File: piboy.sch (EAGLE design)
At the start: 74 parts, among them CN4 MicroUSB, T1 MMUN2133LT1G, U1 TPS61090RSAR, U2 MCP73871

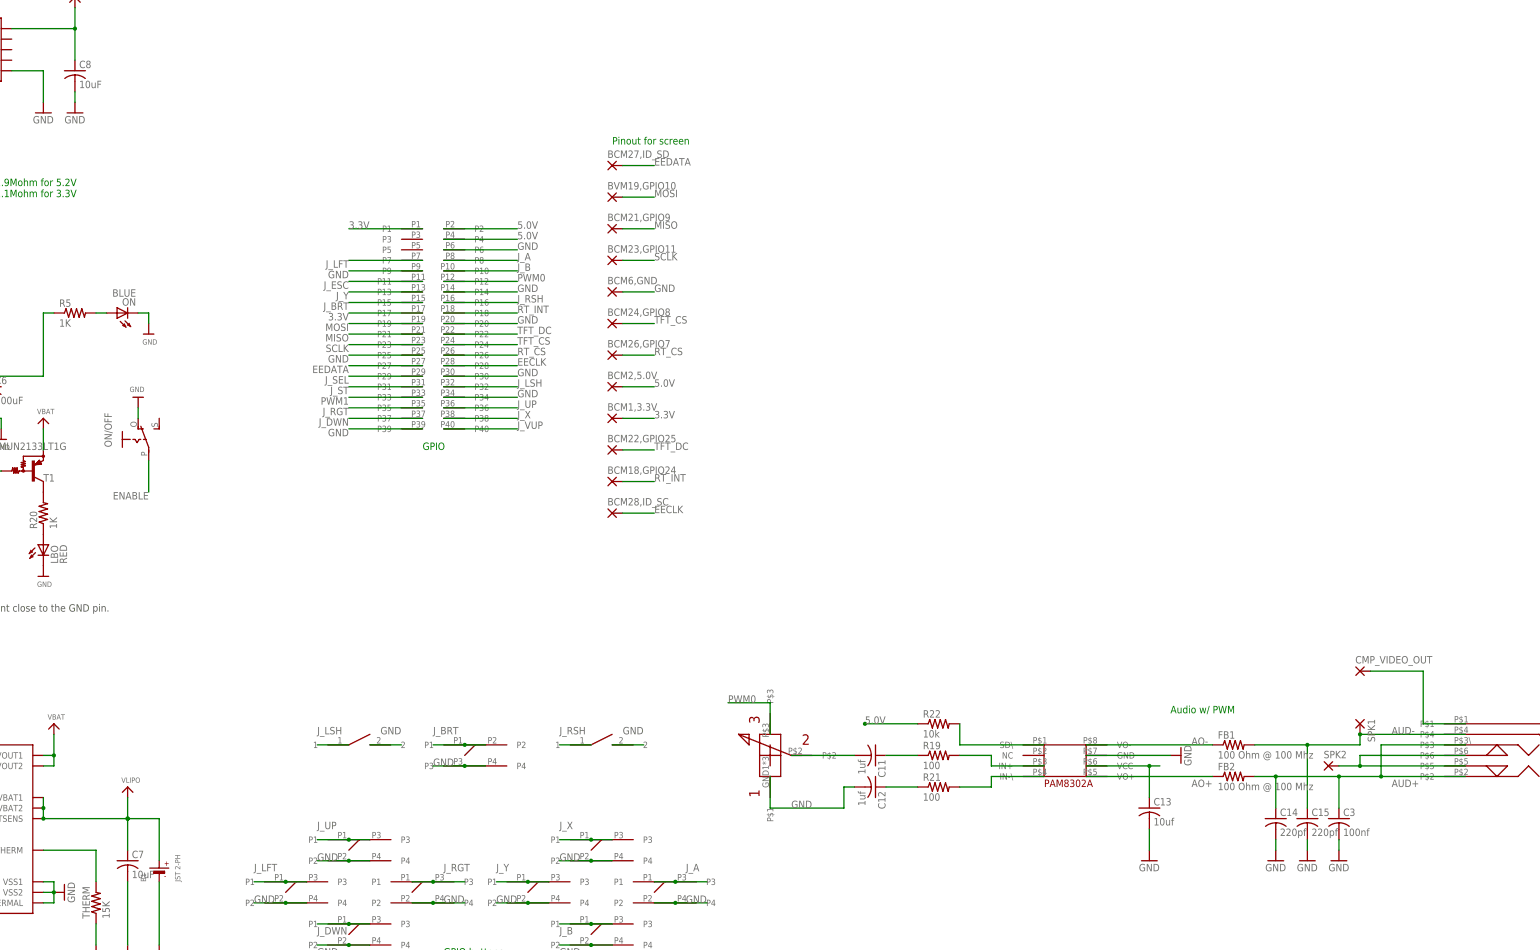
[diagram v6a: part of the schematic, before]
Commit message: -*finally* think I solved the audio issue, redid audio schematic with new parts -started layout
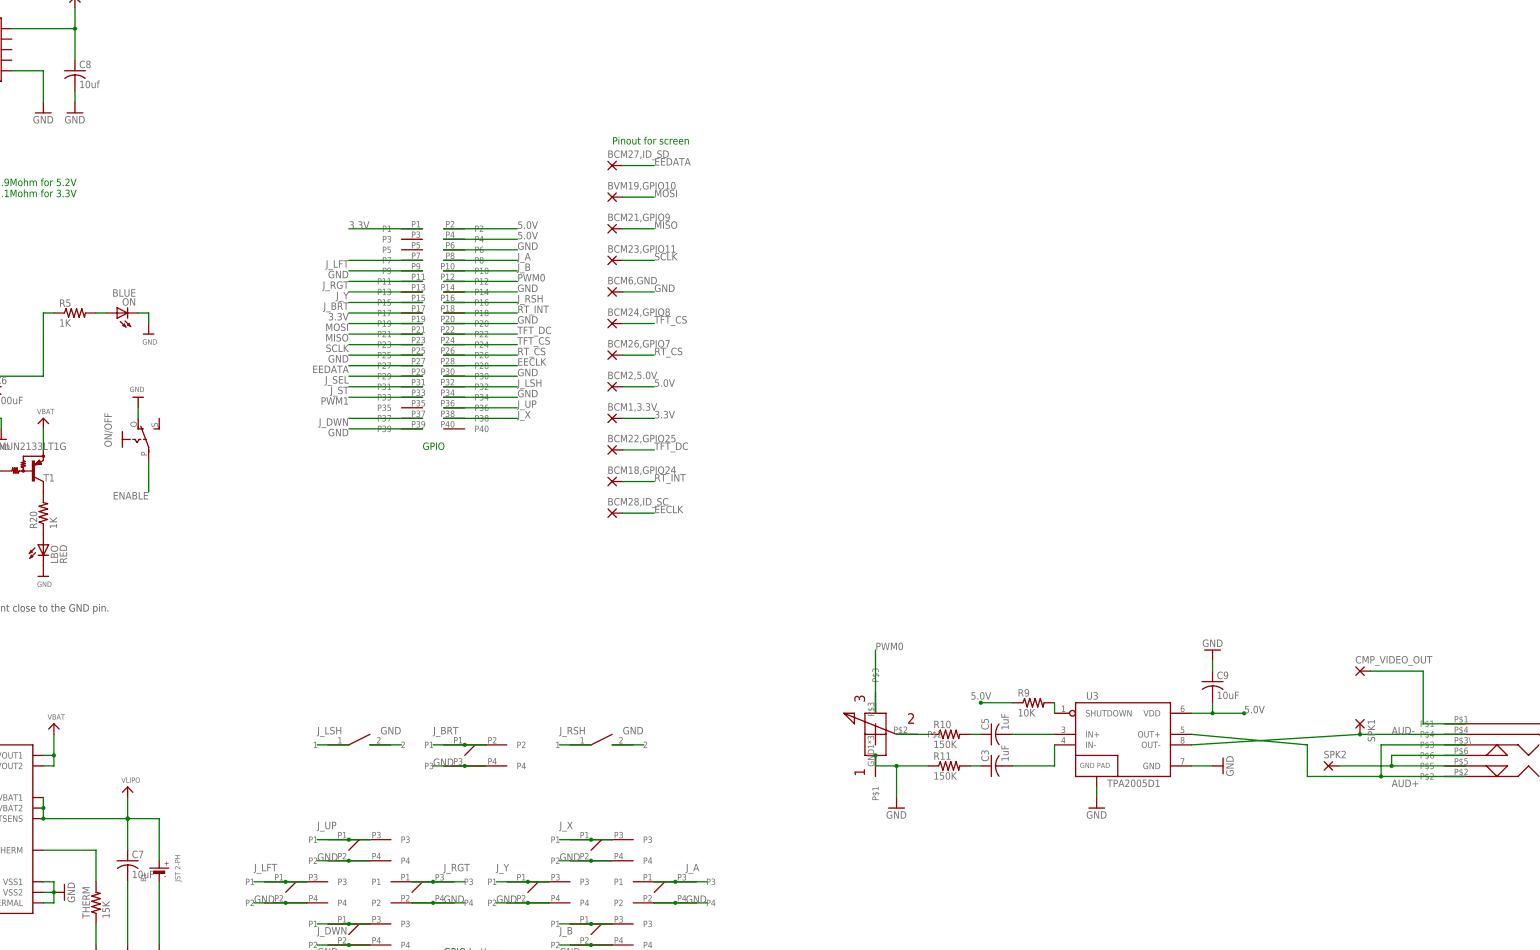
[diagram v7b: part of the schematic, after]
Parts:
- removed C11, C12: 1uf, piboy_new:ADAFRUIT_C-USC0805
- removed C13: 10uf, piboy_new:ADAFRUIT_C-USC0805
- removed C14, C15: 220pf, piboy_new:ADAFRUIT_C-USC0805
- removed FB1, FB2: 100 Ohm @ 100 Mhz, piboy_new:ADAFRUIT_R-US_R0805
- removed R19, R21: 100, piboy_new:ADAFRUIT_R-US_R0805
- removed R22: 10k, piboy_new:ADAFRUIT_R-US_R0805
- removed U$31: PAM8302A, piboy_new:PAM8302A
- added C5: 1uF, resistor:C-USC0805
- added C9: 10uF, resistor:C-USC0805
- added R10, R11: 150K, resistor:R-US_R0805
- added R9: 10K, resistor:R-US_R0805
- added U3: TPA2005D1, SparkFun-IC-Amplifiers:TPA2005D1DGN
- C3: value 100nf -> 1uF; device piboy_new:ADAFRUIT_C-USC0805 -> resistor:C-USC0805
- C8: value 10uF -> 10uf; device piboy_new:ADAFRUIT_C-USC0805 -> adafruit:C-USC0805
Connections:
- removed net AIN+: R19.2, U$31.IN+
- removed net AIN-: R21.2, U$31.IN-\
- removed net AO+: FB2.1, U$31.VO+
- removed net AO-: FB1.1, U$31.VO-
- removed net J_ESC: U$9.P11
- removed net J_VUP: U$9.P40
- removed net N$25: C11.2, U$33.P$2
- removed net SD: R22.2, U$31.SD\
- new net AUD+_HDPN_OUT: SPK2.P, U$40.P$5, U$40.P$6
- new net N$21: C3.1, R11.2
- new net N$22: R10.1, U$33.P$2
- new net N$23: C5.2, U3.IN+
- new net N$26: C3.2, U3.IN-
- net 5.0V: now also C9.2, R9.1, U3.VDD; no longer C13.1, R22.1, U$31.VCC
- net AUD+: now also U3.OUT+; no longer C14.1, C3.1, FB2.2, SPK2.P, U$40.P$5, U$40.P$6
- net AUD-: now also U3.OUT-; no longer C15.1, FB1.2
- net GND: now also C9.1, R11.1, U3.GND@1, U3.GND@2; no longer C12.2, C13.2, C14.2, C15.2, C3.2, U$31.GND
- net J_RGT: now also U$9.P11; no longer U$9.P35
- net N$17: now also R9.2, U3.SHUTDOWN; no longer C12.1, R21.1
- net N$20: now also C5.1, R10.2; no longer C11.1, R19.1
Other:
- note removed: "Audio w/ PWM"

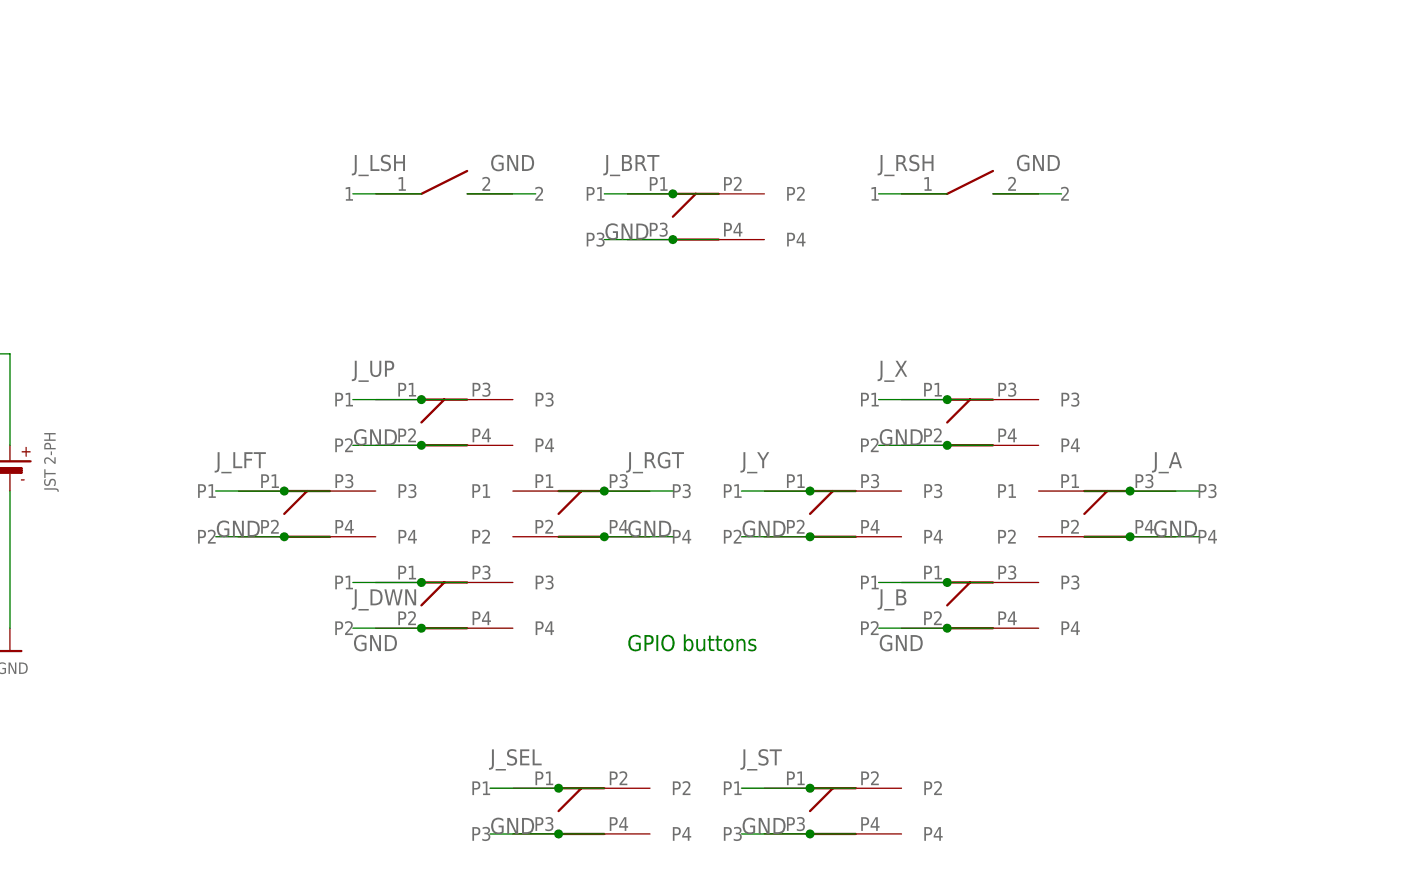
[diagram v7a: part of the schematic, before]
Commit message: -fixed small button pads
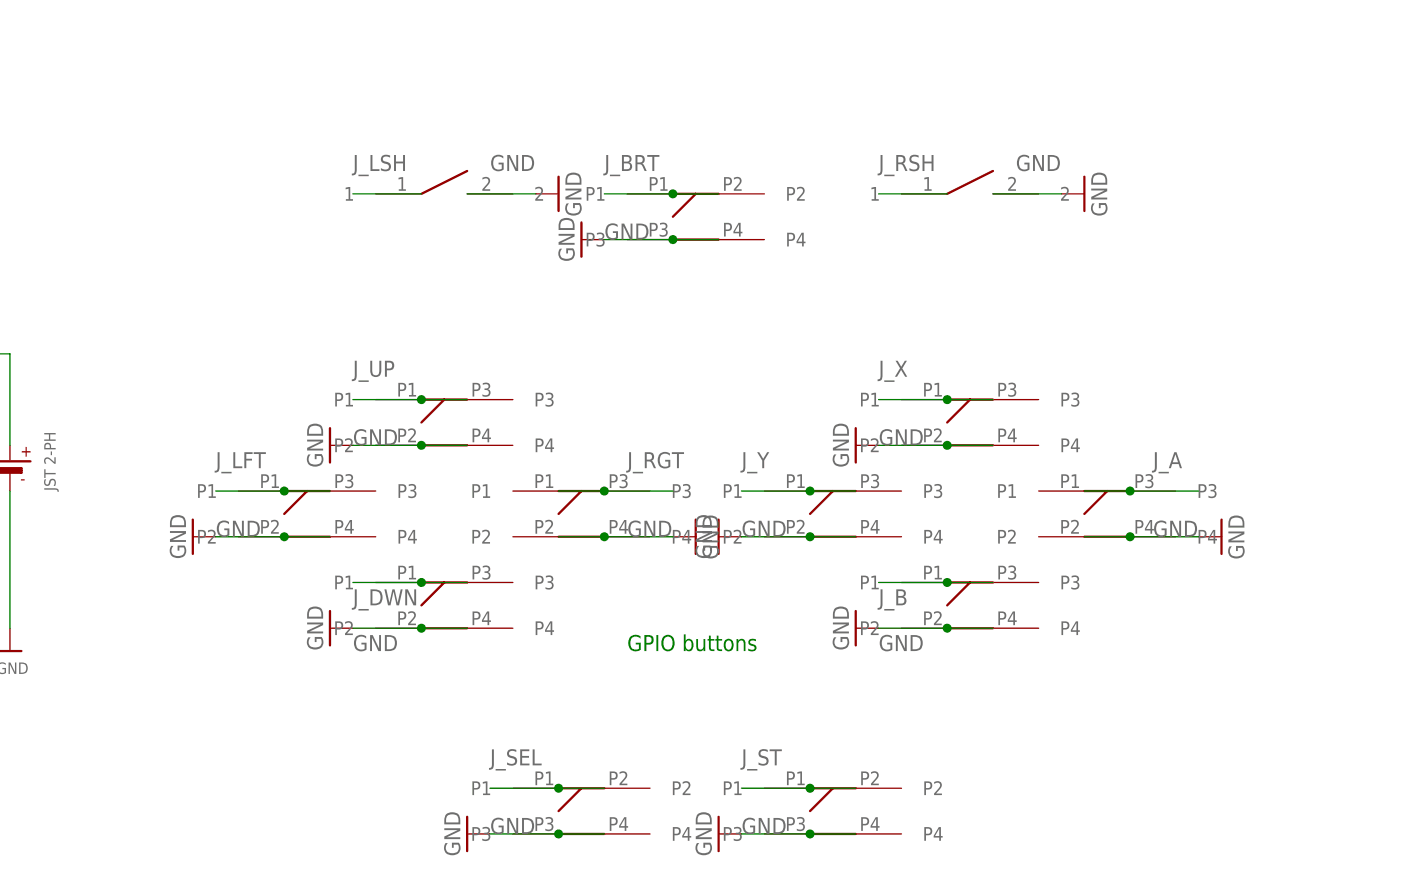
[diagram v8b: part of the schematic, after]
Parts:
- U$21, U$22, U$25: value TL3315NF100Q -> PIBOY_TL3315NF100Q; device piboy:TL3315NF100Q -> piboy_new:PIBOY_TL3315NF100Q
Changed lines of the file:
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@@
 <part name="U$17" library="piboy_new" deviceset="PIBOY_SKRRAAE010" device=""/>
 <part name="U$18" library="piboy_new" deviceset="PIBOY_SKRRAAE010" device=""/>
-<part name="U$21" library="piboy" deviceset="TL3315NF100Q" device=""/>
-<part name="U$22" library="piboy" deviceset="TL3315NF100Q" device=""/>
-<part name="U$25" library="piboy" deviceset="TL3315NF100Q" device=""/>
+<part name="U$21" library="piboy_new" deviceset="PIBOY_TL3315NF100Q" device=""/>
+<part name="U$22" library="piboy_new" deviceset="PIBOY_TL3315NF100Q" device=""/>
+<part name="U$25" library="piboy_new" deviceset="PIBOY_TL3315NF100Q" device=""/>
 <part name="U$26" library="piboy_new" deviceset="SWITCH_TL1105L-4,3" device=""/>
 <part name="U$28" library="piboy_new" deviceset="SWITCH_TL1105L-4,3" device=""/>
@@
 <part name="GND6" library="supply1" deviceset="GND" device=""/>
 <part name="GND7" library="supply1" deviceset="GND" device=""/>
+<part name="GND8" library="supply1" deviceset="GND" device=""/>
+<part name="GND12" library="supply1" deviceset="GND" device=""/>
+<part name="GND13" library="supply1" deviceset="GND" device=""/>
+<part name="GND16" library="supply1" deviceset="GND" device=""/>
+<part name="GND17" library="supply1" deviceset="GND" device=""/>
+<part name="GND18" library="supply1" deviceset="GND" device=""/>
+<part name="GND19" library="supply1" deviceset="GND" device=""/>
+<part name="GND20" library="supply1" deviceset="GND" device=""/>
+<part name="GND21" library="supply1" deviceset="GND" device=""/>
+<part name="GND22" library="supply1" deviceset="GND" device=""/>
+<part name="GND23" library="supply1" deviceset="GND" device=""/>
+<part name="GND24" library="supply1" deviceset="GND" device=""/>
+<part name="GND25" library="supply1" deviceset="GND" device=""/>
 </parts>
 <sheets>
@@
 <instance part="GND6" gate="1" x="185.42" y="-111.76"/>
 <instance part="GND7" gate="1" x="137.16" y="-111.76"/>
+<instance part="GND8" gate="1" x="-5.08" y="-144.78" rot="R270"/>
+<instance part="GND12" gate="1" x="-20.32" y="-134.62" rot="R270"/>
+<instance part="GND13" gate="1" x="35.56" y="-134.62" rot="R90"/>
+<instance part="GND16" gate="1" x="38.1" y="-134.62" rot="R270"/>
+<instance part="GND17" gate="1" x="10.16" y="-167.64" rot="R270"/>
+<instance part="GND18" gate="1" x="38.1" y="-167.64" rot="R270"/>
+<instance part="GND19" gate="1" x="53.34" y="-124.46" rot="R270"/>
+<instance part="GND20" gate="1" x="-5.08" y="-124.46" rot="R270"/>
+<instance part="GND21" gate="1" x="53.34" y="-144.78" rot="R270"/>
+<instance part="GND22" gate="1" x="93.98" y="-134.62" rot="R90"/>
+<instance part="GND23" gate="1" x="22.86" y="-101.6" rot="R270"/>
+<instance part="GND24" gate="1" x="20.32" y="-96.52" rot="R90"/>
+<instance part="GND25" gate="1" x="78.74" y="-96.52" rot="R90"/>
 </instances>
 <busses>
@@
 <wire x1="10.16" y1="-96.52" x2="17.78" y2="-96.52" width="0.1524" layer="91"/>
 <label x="12.7" y="-93.98" size="1.778" layer="95"/>
+<pinref part="GND24" gate="1" pin="GND"/>
 </segment>
 <segment>
@@
 <wire x1="68.58" y1="-96.52" x2="76.2" y2="-96.52" width="0.1524" layer="91"/>
 <label x="71.12" y="-93.98" size="1.778" layer="95"/>
+<pinref part="GND25" gate="1" pin="GND"/>
 </segment>
 <segment>
@@
 <junction x="33.02" y="-101.6"/>
 <label x="25.4" y="-101.6" size="1.778" layer="95"/>
+<pinref part="GND23" gate="1" pin="GND"/>
 </segment>
 <segment>
@@
 <junction x="5.08" y="-124.46"/>
 <label x="-2.54" y="-124.46" size="1.778" layer="95"/>
+<pinref part="GND20" gate="1" pin="GND"/>
 </segment>
 <segment>
@@
 <junction x="-10.16" y="-134.62"/>
 <label x="-17.78" y="-134.62" size="1.778" layer="95"/>
+<pinref part="GND12" gate="1" pin="GND"/>
 </segment>
 <segment>
@@
 <junction x="25.4" y="-134.62"/>
 <label x="27.94" y="-134.62" size="1.778" layer="95"/>
+<pinref part="GND13" gate="1" pin="GND"/>
 </segment>
 <segment>
@@
 <junction x="5.08" y="-144.78"/>
 <label x="-2.54" y="-147.32" size="1.778" layer="95"/>
+<pinref part="GND8" gate="1" pin="GND"/>
 </segment>
 <segment>
@@
 <junction x="63.5" y="-124.46"/>
 <label x="55.88" y="-124.46" size="1.778" layer="95"/>
+<pinref part="GND19" gate="1" pin="GND"/>
 </segment>
 <segment>
@@
 <junction x="48.26" y="-134.62"/>
 <label x="40.64" y="-134.62" size="1.778" layer="95"/>
+<pinref part="GND16" gate="1" pin="GND"/>
 </segment>
 <segment>
@@
 <junction x="83.82" y="-134.62"/>
 <label x="86.36" y="-134.62" size="1.778" layer="95"/>
+<pinref part="GND22" gate="1" pin="GND"/>
 </segment>
 <segment>
@@
 <junction x="63.5" y="-144.78"/>
 <label x="55.88" y="-147.32" size="1.778" layer="95"/>
+<pinref part="GND21" gate="1" pin="GND"/>
 </segment>
 <segment>
@@
 <junction x="20.32" y="-167.64"/>
 <label x="12.7" y="-167.64" size="1.778" layer="95"/>
+<pinref part="GND17" gate="1" pin="GND"/>
 </segment>
 <segment>
@@
 <junction x="48.26" y="-167.64"/>
 <label x="40.64" y="-167.64" size="1.778" layer="95"/>
-</segment>
-<segment>
+<pinref part="GND18" gate="1" pin="GND"/>
+</segment>
+<segment>
